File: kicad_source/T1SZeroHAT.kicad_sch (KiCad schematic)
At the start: 44 parts, among them CN1 RASPI-IO, CN2 XY2500R-F-3.81-2P, CN3 SM02B-GHS-TB, CN4 SM02B-GHS-TB, SW1 SS-3235S-L3, U1 LAN8651, Y1 X1E0000210808

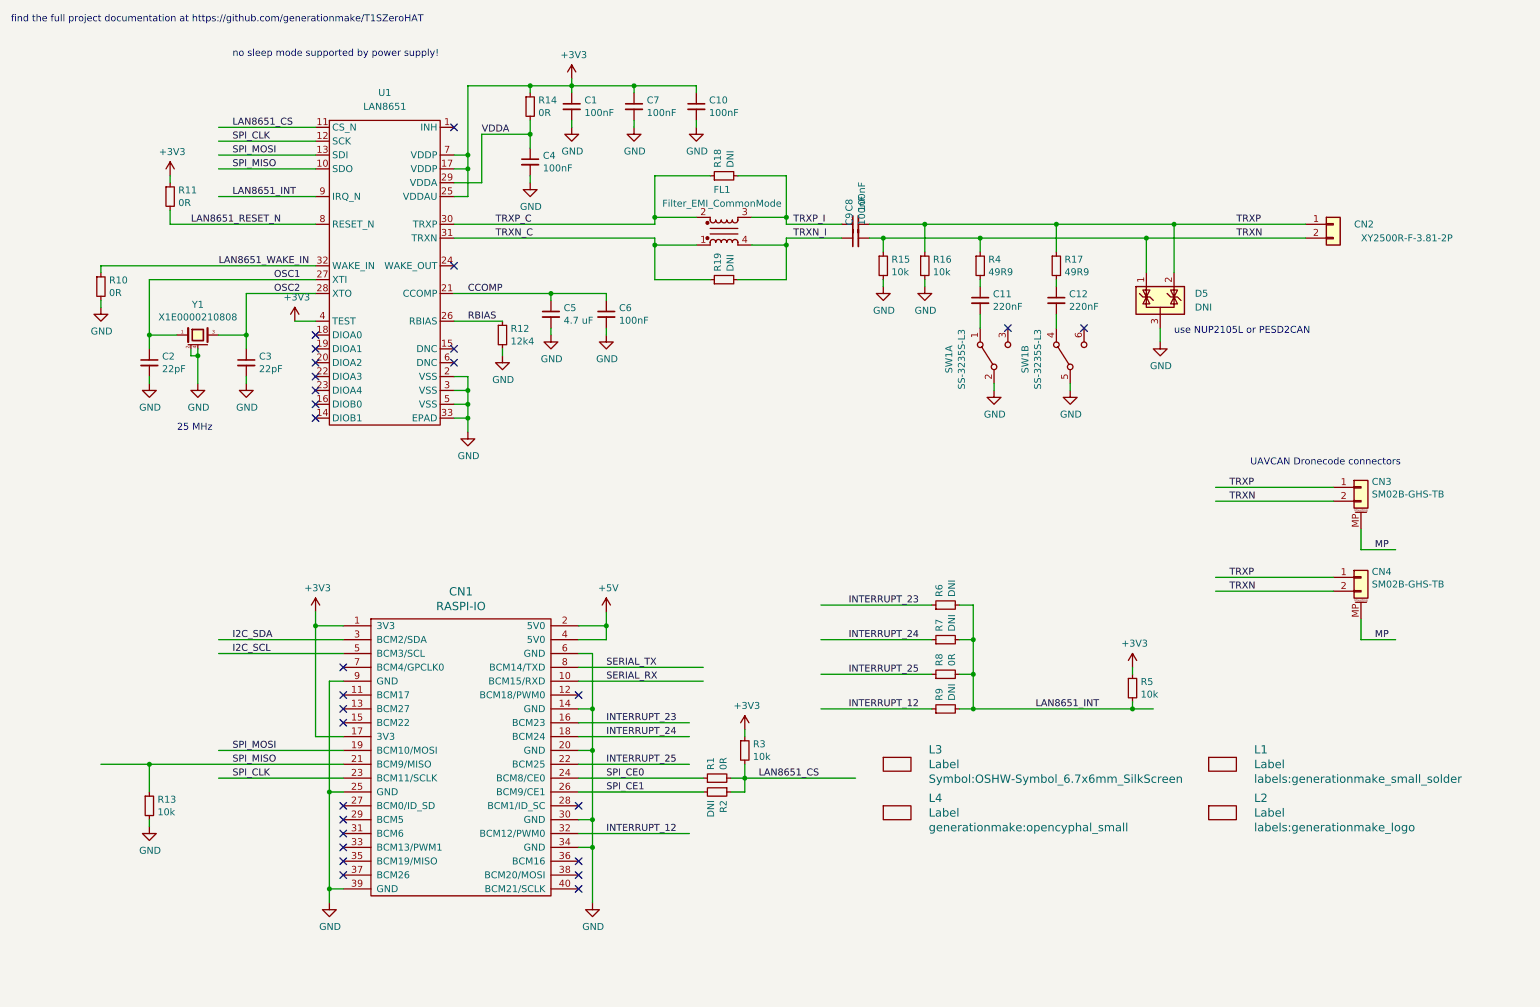
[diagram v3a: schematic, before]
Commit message: updated schematic for power delivery
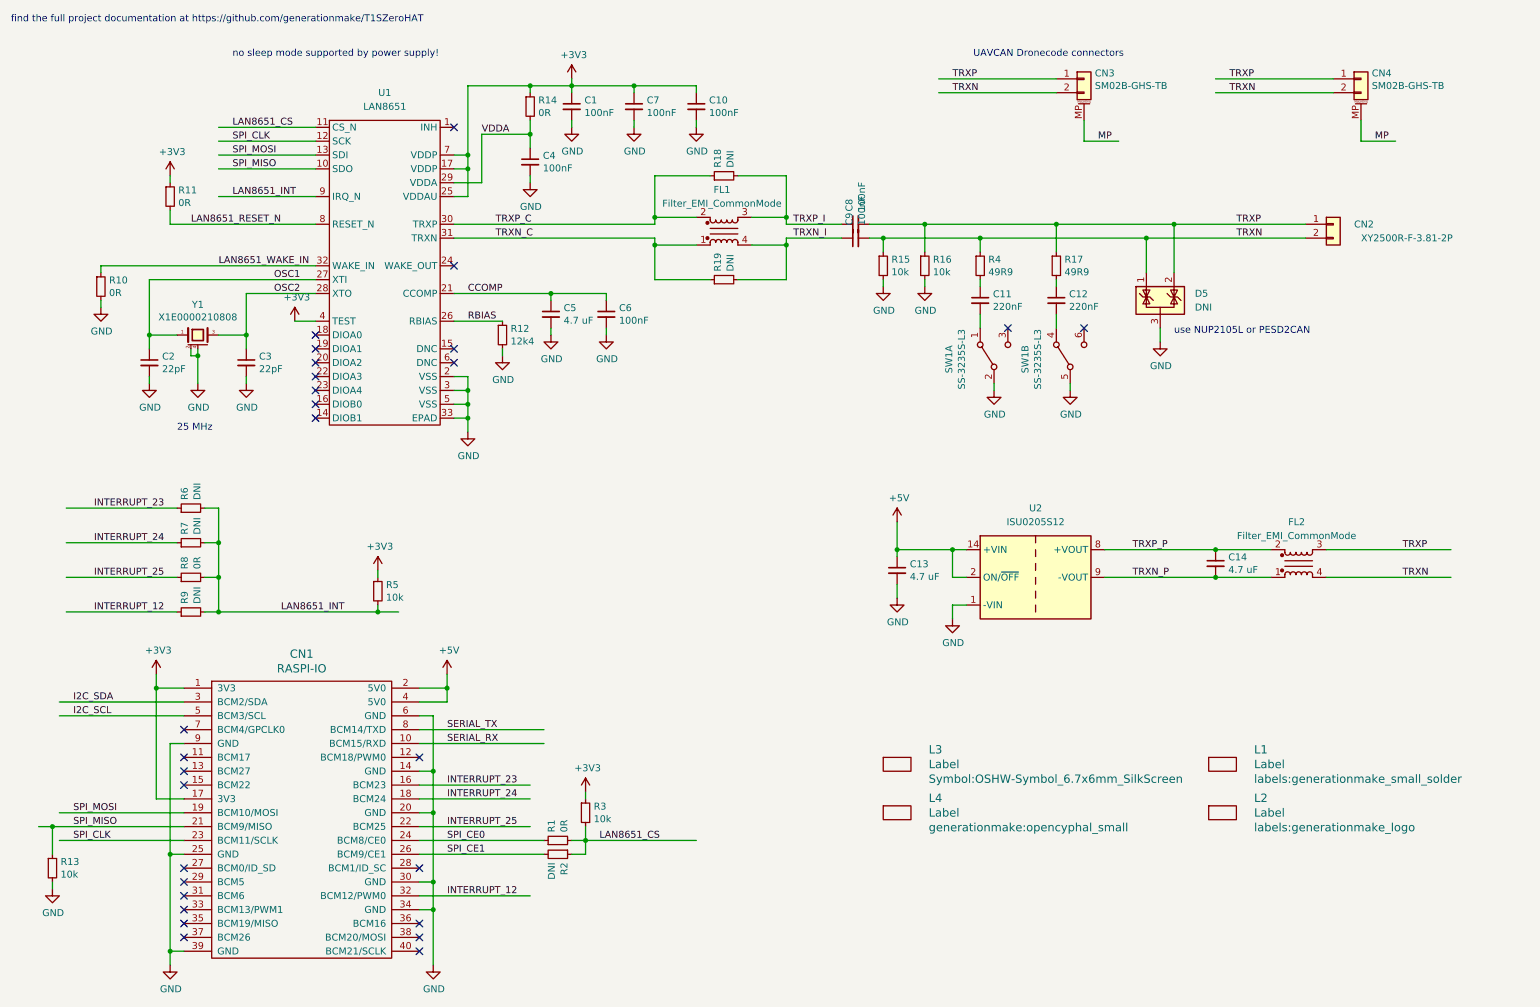
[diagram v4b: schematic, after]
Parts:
- added C13, C14: 4.7 uF, Capacitor_SMD:C_0603_1608Metric, symbol Device:C_Small
- added FL2: Filter_EMI_CommonMode, Filter:Filter_Bourns_SRF0905_6.0x9.2mm, symbol Device:Filter_EMI_LL_1423
- added U2: ISU0205S12, Converter_DCDC:Converter_DCDC_XP_POWER-ISU02_SMD, symbol Converter_DCDC:ISU0205S12
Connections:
- net +5V: now also C13.1, U2.14 (+VIN), U2.2 (ON/~{OFF})
- net GND: now also C13.2, U2.1 (-VIN)
- net TRXN: now also FL2.4
- net TRXP: now also FL2.3
- new net TRXN_P: C14.2, FL2.1, U2.9 (-VOUT)
- new net TRXP_P: C14.1, FL2.2, U2.8 (+VOUT)
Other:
- moved on the sheet: CN1, CN3, CN4, R1, R13, R2, R3, R5, R6, R7, R8, R9

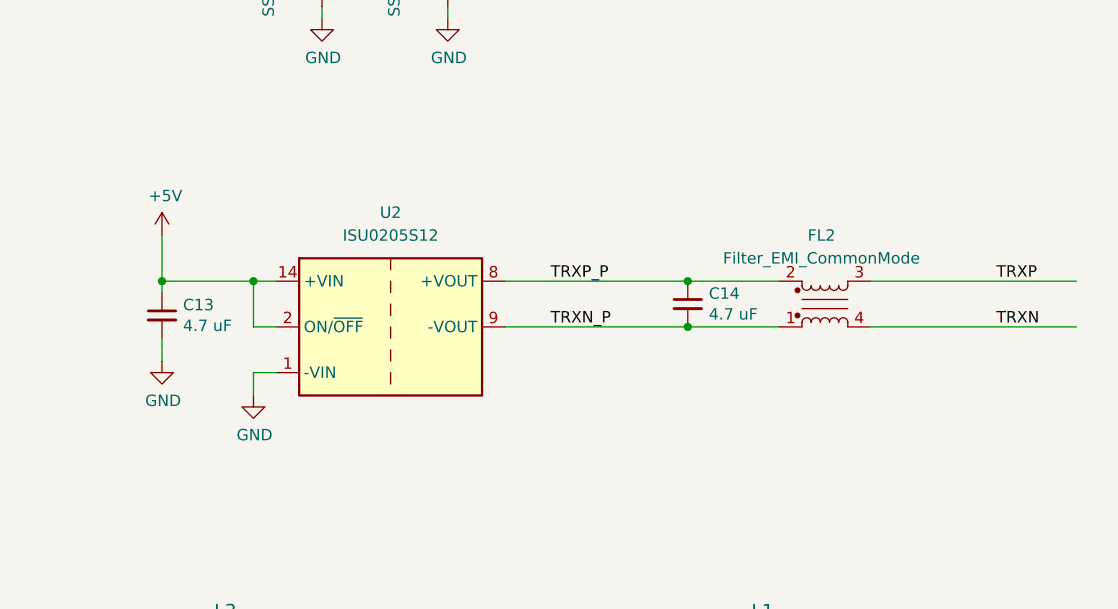
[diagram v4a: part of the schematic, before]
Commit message: updated layout for power delivery
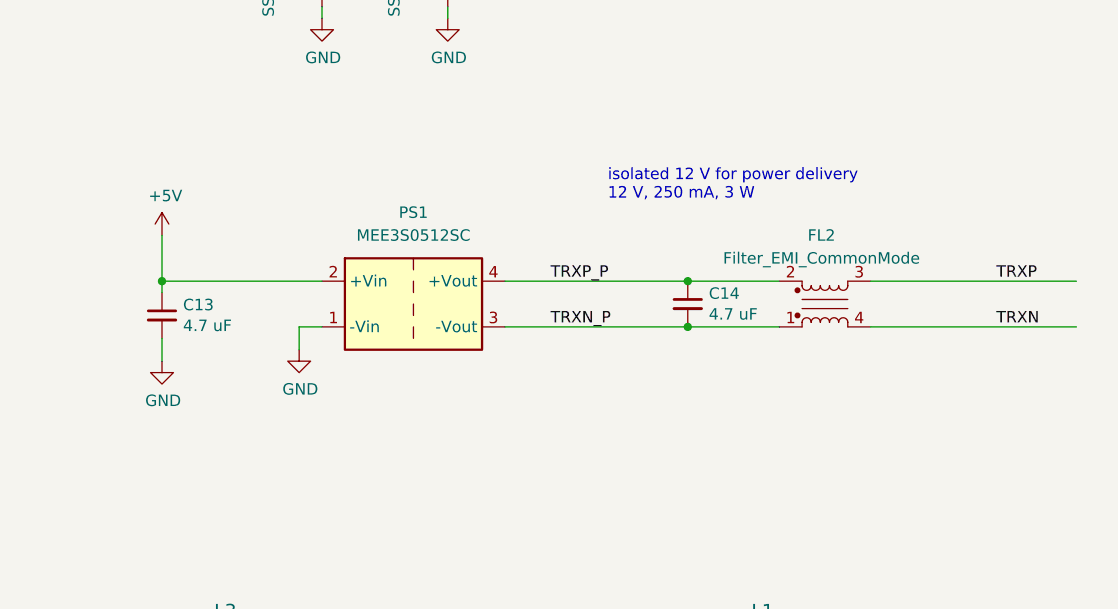
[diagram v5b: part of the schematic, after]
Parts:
- removed U2: ISU0205S12, Converter_DCDC:Converter_DCDC_XP_POWER-ISU02_SMD, symbol Converter_DCDC:ISU0205S12
- added PS1: MEE3S0512SC, Converter_DCDC:Converter_DCDC_Murata_MEE3SxxxxSC_THT, symbol Converter_DCDC:MEE3S0512SC
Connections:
- net +5V: now also PS1.2 (+Vin)
- net GND: now also PS1.1 (-Vin)
- net TRXN_P: now also PS1.3 (-Vout)
- net TRXP_P: now also PS1.4 (+Vout)
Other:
- note added: "isolated 12 V for power delivery 12 V, 250 mA, 3 W"
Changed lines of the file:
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@@
   (junction (at 154.94 50.8) (diameter 0) (color 0 0 0 0)
-  )
-  (junction (at 185.42 111.76) (diameter 0) (color 0 0 0 0)
   )
   (junction (at 204.47 52.07) (diameter 0) (color 0 0 0 0)
@@
     (stroke (width 0) (type default) (color 0 0 0 0))
   )
+  (wire (pts (xy 190.5 116.84) (xy 190.5 119.38))
+    (stroke (width 0) (type default) (color 0 0 0 0))
+  )
   (wire (pts (xy 220.98 54.61) (xy 250.19 54.61))
     (stroke (width 0) (type default) (color 0 0 0 0))
@@
     (stroke (width 0) (type default) (color 0 0 0 0))
   )
+  (wire (pts (xy 193.04 116.84) (xy 190.5 116.84))
+    (stroke (width 0) (type default) (color 0 0 0 0))
+  )
   (wire (pts (xy 209.55 33.02) (xy 209.55 36.83))
     (stroke (width 0) (type default) (color 0 0 0 0))
@@
     (stroke (width 0) (type default) (color 0 0 0 0))
   )
-  (wire (pts (xy 185.42 121.92) (xy 185.42 124.46))
-    (stroke (width 0) (type default) (color 0 0 0 0))
-  )
   (wire (pts (xy 204.47 52.07) (xy 204.47 57.15))
     (stroke (width 0) (type default) (color 0 0 0 0))
@@
     (stroke (width 0) (type default) (color 0 0 0 0))
   )
-  (wire (pts (xy 185.42 116.84) (xy 185.42 111.76))
-    (stroke (width 0) (type default) (color 0 0 0 0))
-  )
   (wire (pts (xy 50.8 34.29) (xy 68.58 34.29))
     (stroke (width 0) (type default) (color 0 0 0 0))
@@
     (stroke (width 0) (type default) (color 0 0 0 0))
   )
-  (wire (pts (xy 175.26 111.76) (xy 185.42 111.76))
-    (stroke (width 0) (type default) (color 0 0 0 0))
-  )
   (wire (pts (xy 93.98 85.09) (xy 96.52 85.09))
     (stroke (width 0) (type default) (color 0 0 0 0))
@@
     (stroke (width 0) (type default) (color 0 0 0 0))
   )
-  (wire (pts (xy 187.96 121.92) (xy 185.42 121.92))
-    (stroke (width 0) (type default) (color 0 0 0 0))
-  )
   (wire (pts (xy 90.17 152.4) (xy 90.17 160.02))
     (stroke (width 0) (type default) (color 0 0 0 0))
@@
     (stroke (width 0) (type default) (color 0 0 0 0))
   )
-  (wire (pts (xy 187.96 116.84) (xy 185.42 116.84))
-    (stroke (width 0) (type default) (color 0 0 0 0))
-  )
   (wire (pts (xy 154.94 43.18) (xy 146.05 43.18))
     (stroke (width 0) (type default) (color 0 0 0 0))
@@
     (stroke (width 0) (type default) (color 0 0 0 0))
   )
-  (wire (pts (xy 185.42 111.76) (xy 187.96 111.76))
+  (wire (pts (xy 175.26 111.76) (xy 193.04 111.76))
     (stroke (width 0) (type default) (color 0 0 0 0))
   )
@@
   (wire (pts (xy 99.06 44.45) (xy 99.06 35.56))
     (stroke (width 0) (type default) (color 0 0 0 0))
+  )
+  (text "isolated 12 V for power delivery\n12 V, 250 mA, 3 W"
+    (at 224.79 102.87 0)
+    (effects (font (size 1.27 1.27)) (justify left bottom))
   )
   (text "find the full project documentation at https://github.com/generationmake/T1SZeroHAT"
@@
     (pin "2")
   )
-  (symbol (lib_id "Converter_DCDC:ISU0205S12") (at 200.66 116.84 0) (unit 1)
-    (in_bom yes) (on_board yes) (fields_autoplaced)
-    (property "Reference" "U2" (id 0) (at 200.66 104.14 0))
-    (property "Value" "ISU0205S12" (id 1) (at 200.66 106.68 0))
-    (property "Footprint" "Converter_DCDC:Converter_DCDC_XP_POWER-ISU02_SMD" (id 2) (at 200.66 125.73 0)
-      (effects (font (size 1.27 1.27) italic) hide)
-    )
-    (property "Datasheet" "https://www.xppower.com/Portals/0/pdfs/SF_ISU02.pdf" (id 3) (at 200.66 128.27 0)
-      (effects (font (size 1.27 1.27)) hide)
-    )
-    (pin "1")
-    (pin "14")
-    (pin "2")
-    (pin "6")
-    (pin "7")
-    (pin "8")
-    (pin "9")
-  )
   (symbol (lib_id "power:GND") (at 172.72 63.5 0) (unit 1)
     (in_bom yes) (on_board yes)
@@
     (pin "1")
     (pin "2")
+  )
+  (symbol (lib_id "Converter_DCDC:MEE3S0512SC") (at 203.2 114.3 0) (unit 1)
+    (in_bom yes) (on_board yes) (fields_autoplaced)
+    (property "Reference" "PS1" (id 0) (at 203.2 104.14 0))
+    (property "Value" "MEE3S0512SC" (id 1) (at 203.2 106.68 0))
+    (property "Footprint" "Converter_DCDC:Converter_DCDC_Murata_MEE3SxxxxSC_THT" (id 2) (at 176.53 120.65 0)
+      (effects (font (size 1.27 1.27)) (justify left) hide)
+    )
+    (property "Datasheet" "https://power.murata.com/pub/data/power/ncl/kdc_mee3.pdf" (id 3) (at 229.87 121.92 0)
+      (effects (font (size 1.27 1.27)) (justify left) hide)
+    )
+    (pin "1")
+    (pin "2")
+    (pin "3")
+    (pin "4")
   )
   (symbol (lib_id "Device:R_Small") (at 180.34 59.69 0) (unit 1)
@@
     (pin "2")
   )
-  (symbol (lib_id "power:GND") (at 185.42 124.46 0) (unit 1)
-    (in_bom yes) (on_board yes)
-    (property "Reference" "#PWR026" (id 0) (at 185.42 130.81 0)
-      (effects (font (size 1.27 1.27)) hide)
-    )
-    (property "Value" "GND" (id 1) (at 185.547 128.8542 0))
-    (property "Footprint" "" (id 2) (at 185.42 124.46 0))
-    (property "Datasheet" "" (id 3) (at 185.42 124.46 0))
+  (symbol (lib_id "power:GND") (at 190.5 119.38 0) (unit 1)
+    (in_bom yes) (on_board yes)
+    (property "Reference" "#PWR026" (id 0) (at 190.5 125.73 0)
+      (effects (font (size 1.27 1.27)) hide)
+    )
+    (property "Value" "GND" (id 1) (at 190.627 123.7742 0))
+    (property "Footprint" "" (id 2) (at 190.5 119.38 0))
+    (property "Datasheet" "" (id 3) (at 190.5 119.38 0))
     (pin "1")
   )
@@
       (reference "L4") (unit 1) (value "Label") (footprint "generationmake:opencyphal_small")
     )
+    (path "/808d7045-9f31-4126-a848-c4713148cf3d"
+      (reference "PS1") (unit 1) (value "MEE3S0512SC") (footprint "Converter_DCDC:Converter_DCDC_Murata_MEE3SxxxxSC_THT")
+    )
     (path "/00000000-0000-0000-0000-00005fd836f1"
       (reference "R1") (unit 1) (value "0R") (footprint "Resistor_SMD:R_0603_1608Metric")
@@
       (reference "U1") (unit 1) (value "LAN8651") (footprint "Package_DFN_QFN:QFN-32-1EP_5x5mm_P0.5mm_EP3.45x3.45mm")
     )
-    (path "/40a5c827-b9d0-44a7-8044-9dfa8113cfc0"
-      (reference "U2") (unit 1) (value "ISU0205S12") (footprint "Converter_DCDC:Converter_DCDC_XP_POWER-ISU02_SMD")
-    )
     (path "/00000000-0000-0000-0000-00005fd751a0"

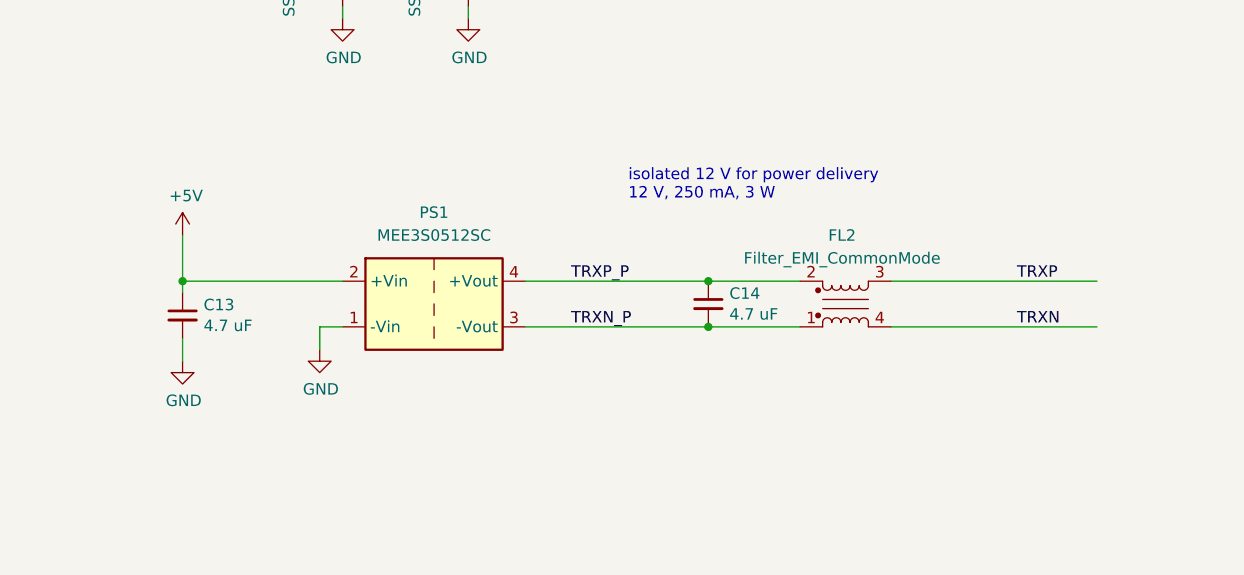
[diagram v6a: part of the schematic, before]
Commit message: removed power delivery parts since they are not specified
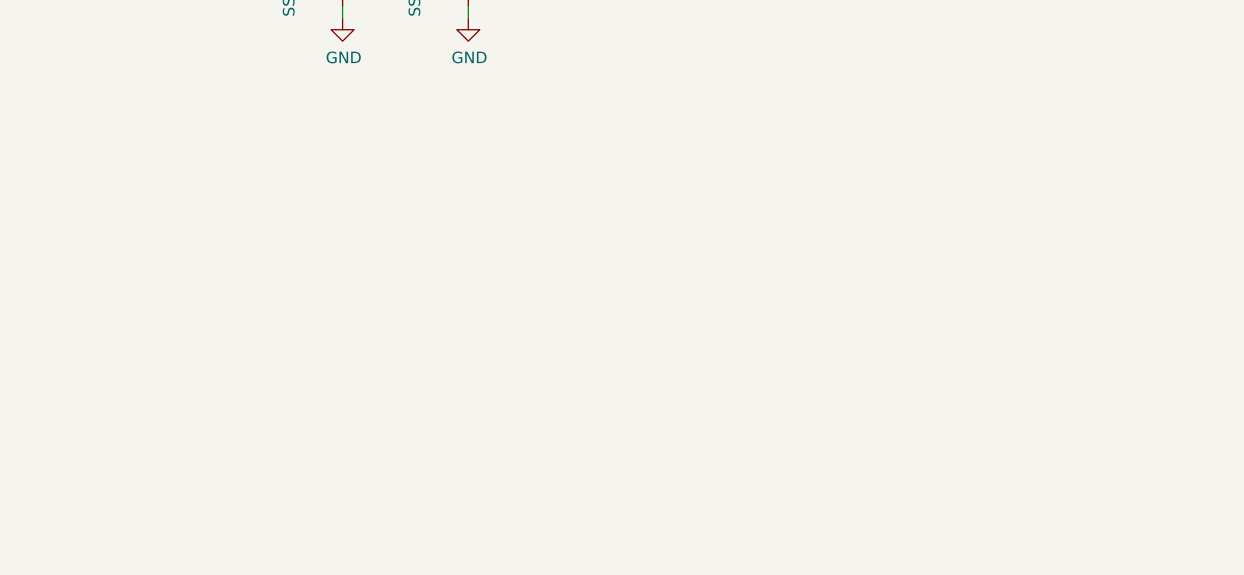
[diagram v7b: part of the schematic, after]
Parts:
- removed C13, C14: 4.7 uF, Capacitor_SMD:C_0603_1608Metric, symbol Device:C_Small
- removed FL2: Filter_EMI_CommonMode, Filter:Filter_Bourns_SRF0905_6.0x9.2mm, symbol Device:Filter_EMI_LL_1423
- removed PS1: MEE3S0512SC, Converter_DCDC:Converter_DCDC_Murata_MEE3SxxxxSC_THT, symbol Converter_DCDC:MEE3S0512SC
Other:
- note removed: "isolated 12 V for power delivery 12 V, 250 mA, 3 W"

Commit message: changed R14..R17 to 1206 according to microchip reference schematic
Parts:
- R15, R16, R17, R4: footprint Resistor_SMD:R_0603_1608Metric -> Resistor_SMD:R_1206_3216Metric
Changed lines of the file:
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@@
 			)
 		)
-		(property "Footprint" "Resistor_SMD:R_0603_1608Metric"
+		(property "Footprint" "Resistor_SMD:R_1206_3216Metric"
 			(at 190.5 63.5 0)
 			(effects
@@
 			)
 		)
-		(property "Footprint" "Resistor_SMD:R_0603_1608Metric"
+		(property "Footprint" "Resistor_SMD:R_1206_3216Metric"
 			(at 172.72 63.5 0)
 			(effects
@@
 			)
 		)
-		(property "Footprint" "Resistor_SMD:R_0603_1608Metric"
+		(property "Footprint" "Resistor_SMD:R_1206_3216Metric"
 			(at 180.34 63.5 0)
 			(effects
@@
 			)
 		)
-		(property "Footprint" "Resistor_SMD:R_0603_1608Metric"
+		(property "Footprint" "Resistor_SMD:R_1206_3216Metric"
 			(at 204.47 63.5 0)
 			(effects
